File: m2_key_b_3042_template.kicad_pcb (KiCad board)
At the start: 2 copper layers, 42 x 30 mm, 5 parts, among them J1 M.2_Key_B

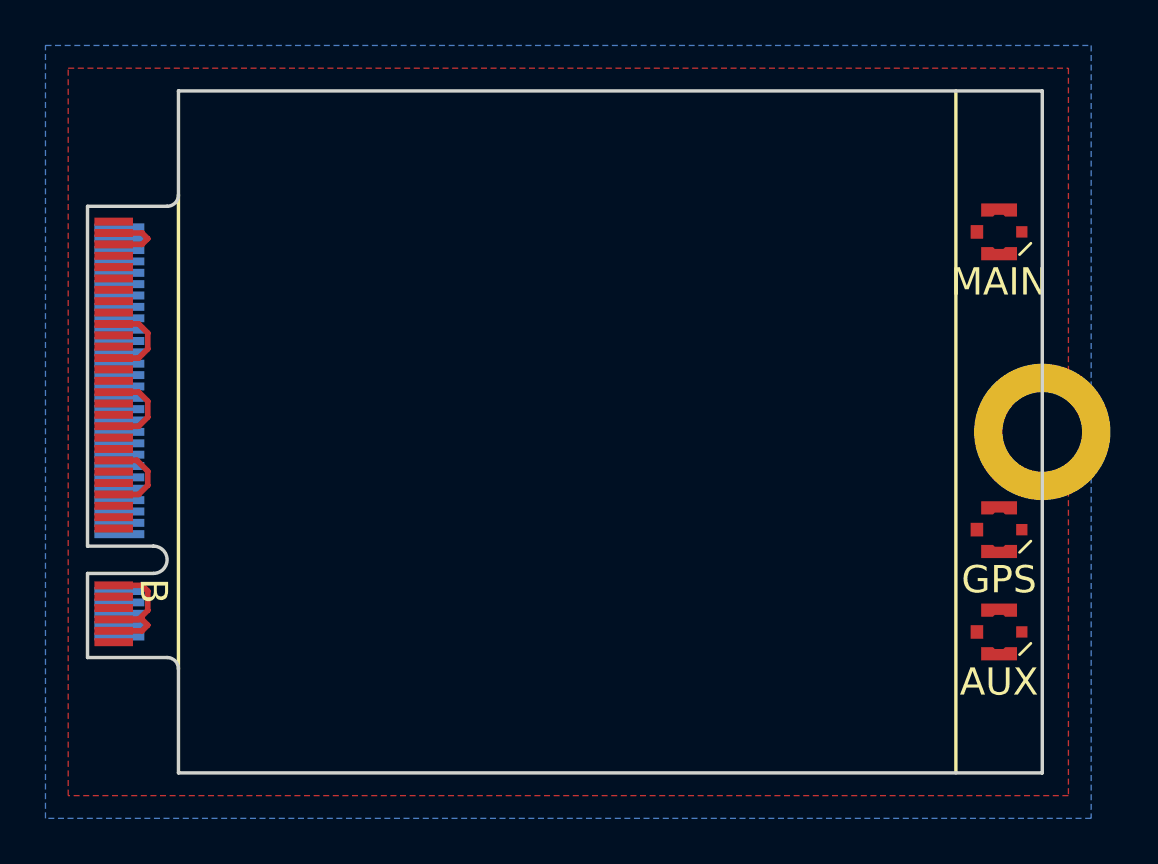
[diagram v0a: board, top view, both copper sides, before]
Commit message: Include copper zones which control the 50Ohm coplanar waveguide for the antennae.
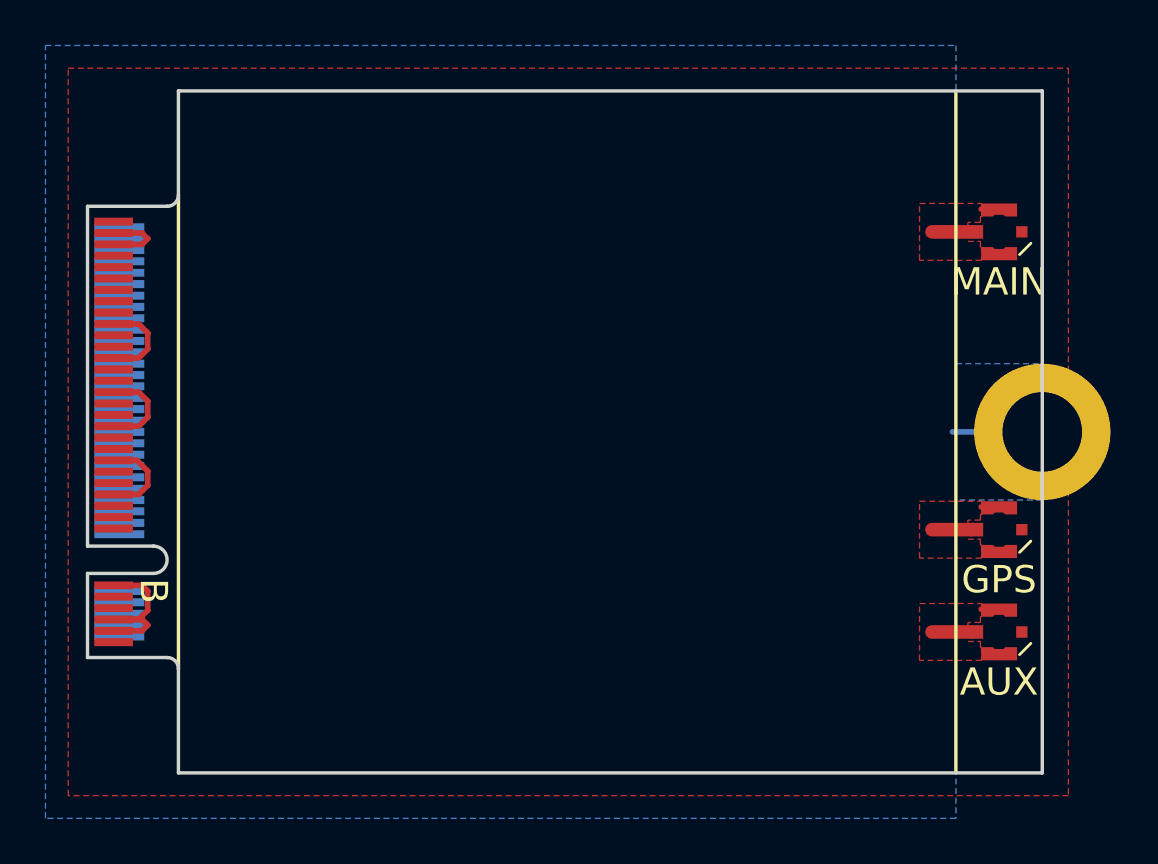
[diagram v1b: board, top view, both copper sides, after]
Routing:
- net GND: track 25.4 -> 28.9 mm
- net /MAIN: track 0.00 -> 1.97 mm
- net /GPS: track 0.00 -> 1.97 mm
- net /AUX: track 0.00 -> 1.97 mm
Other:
- net class Antennae added: clearance 0.12, trace_width 0.25, via_dia 0.6, via_drill 0.4

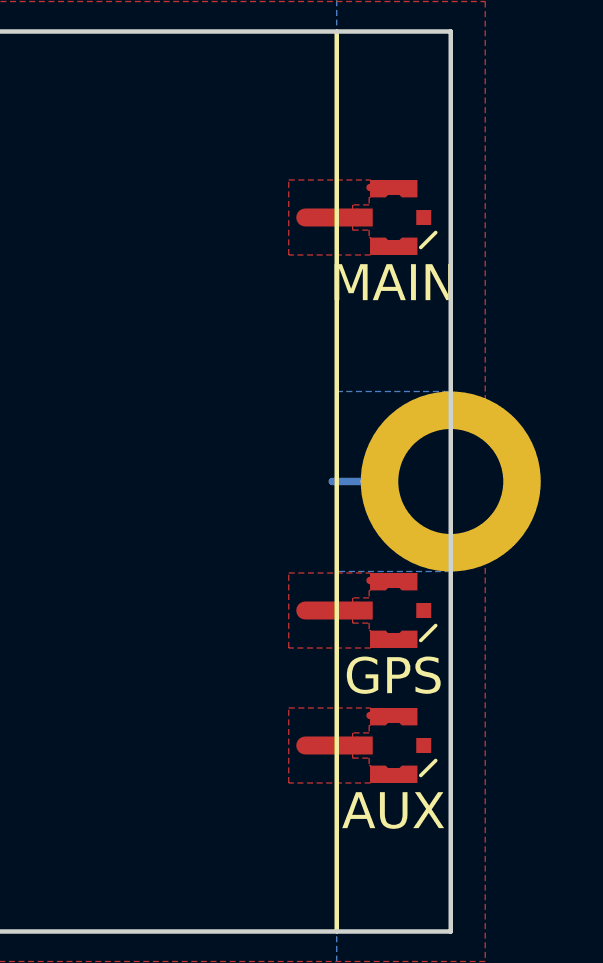
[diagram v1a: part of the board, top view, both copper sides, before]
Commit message: Fix unconnected ground nets on MHF4 connectors.
DRC no longer complains about the polygon shaped GND pads of the MHF4 footprints.
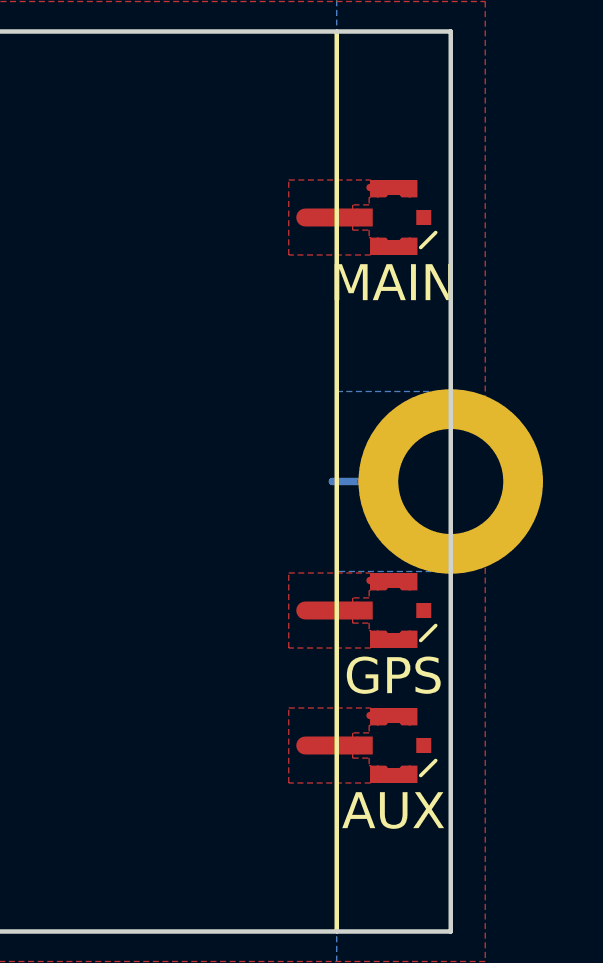
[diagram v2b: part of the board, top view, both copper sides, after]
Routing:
- net GND: track 28.9 -> 31.9 mm
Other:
- rule trace_min: 0.2 -> 0.1524
- rule via_min_drill: 0.3 -> 0.254
- rule via_min_size: 0.4 -> 0.508
